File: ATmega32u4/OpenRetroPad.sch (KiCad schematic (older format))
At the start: 48 parts, among them J1 USB_B_Micro, J2 NRF24, J3 DB25_Female_MountingHoles, SW1 SW_Push, SW2 SW_Push, U1 AMS1117-3.3, U2 ATmega32U4, Y1 16MHz

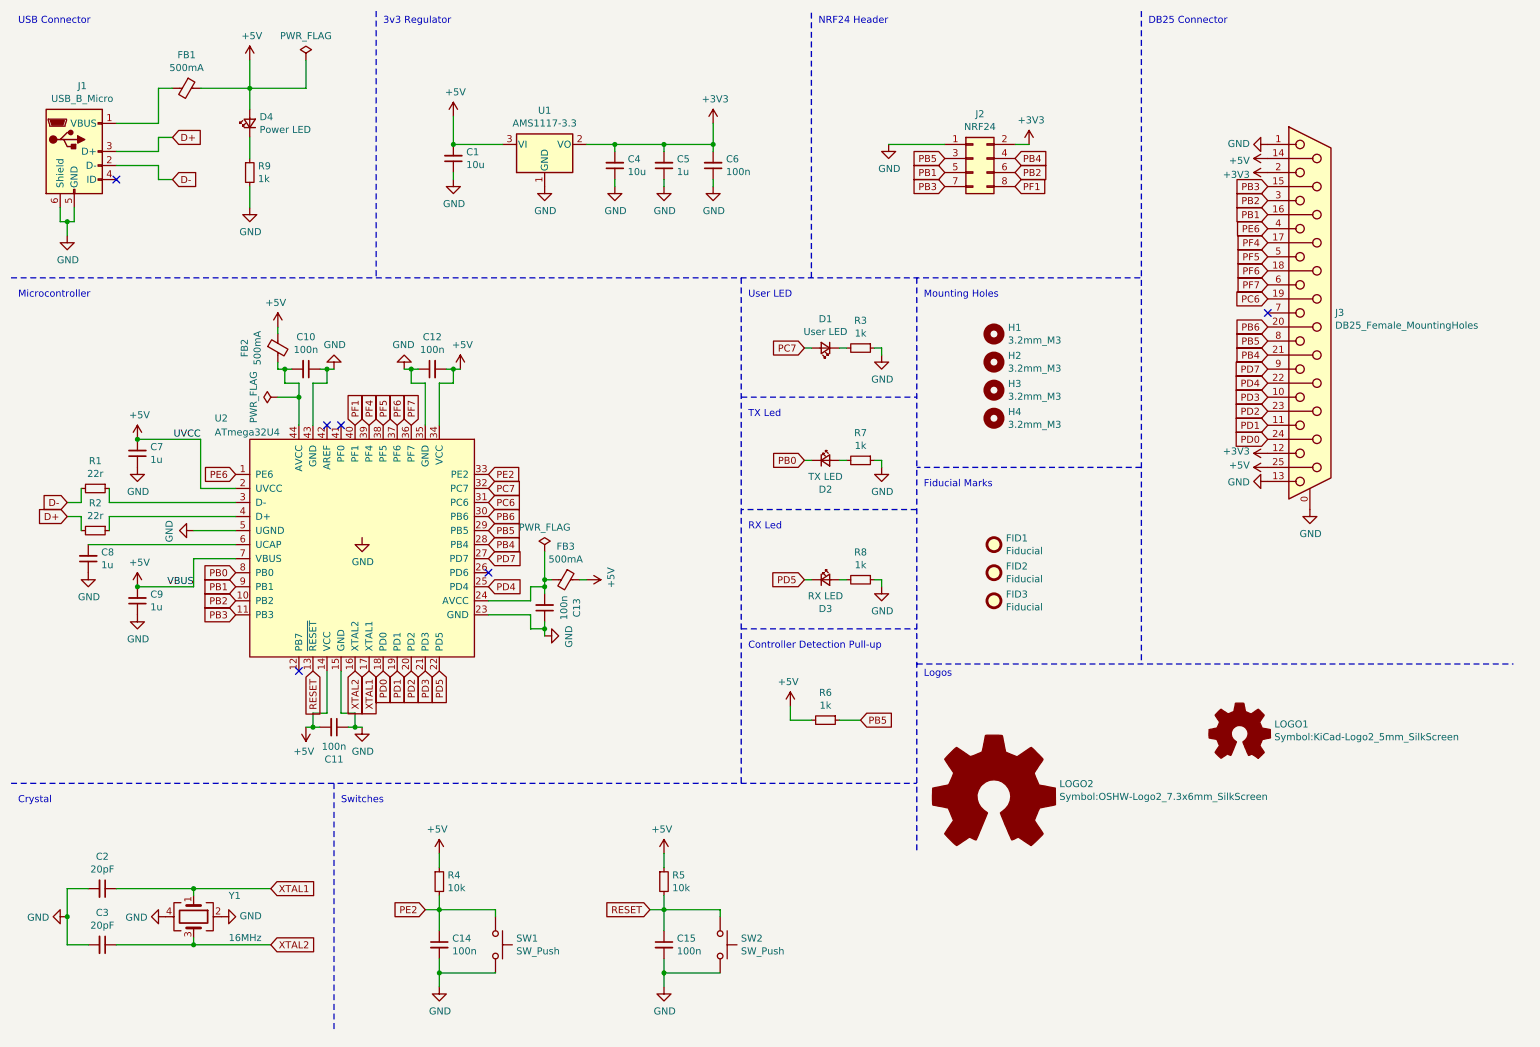
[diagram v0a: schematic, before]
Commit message: Update 2 layer board and use 0805 components, include outputs
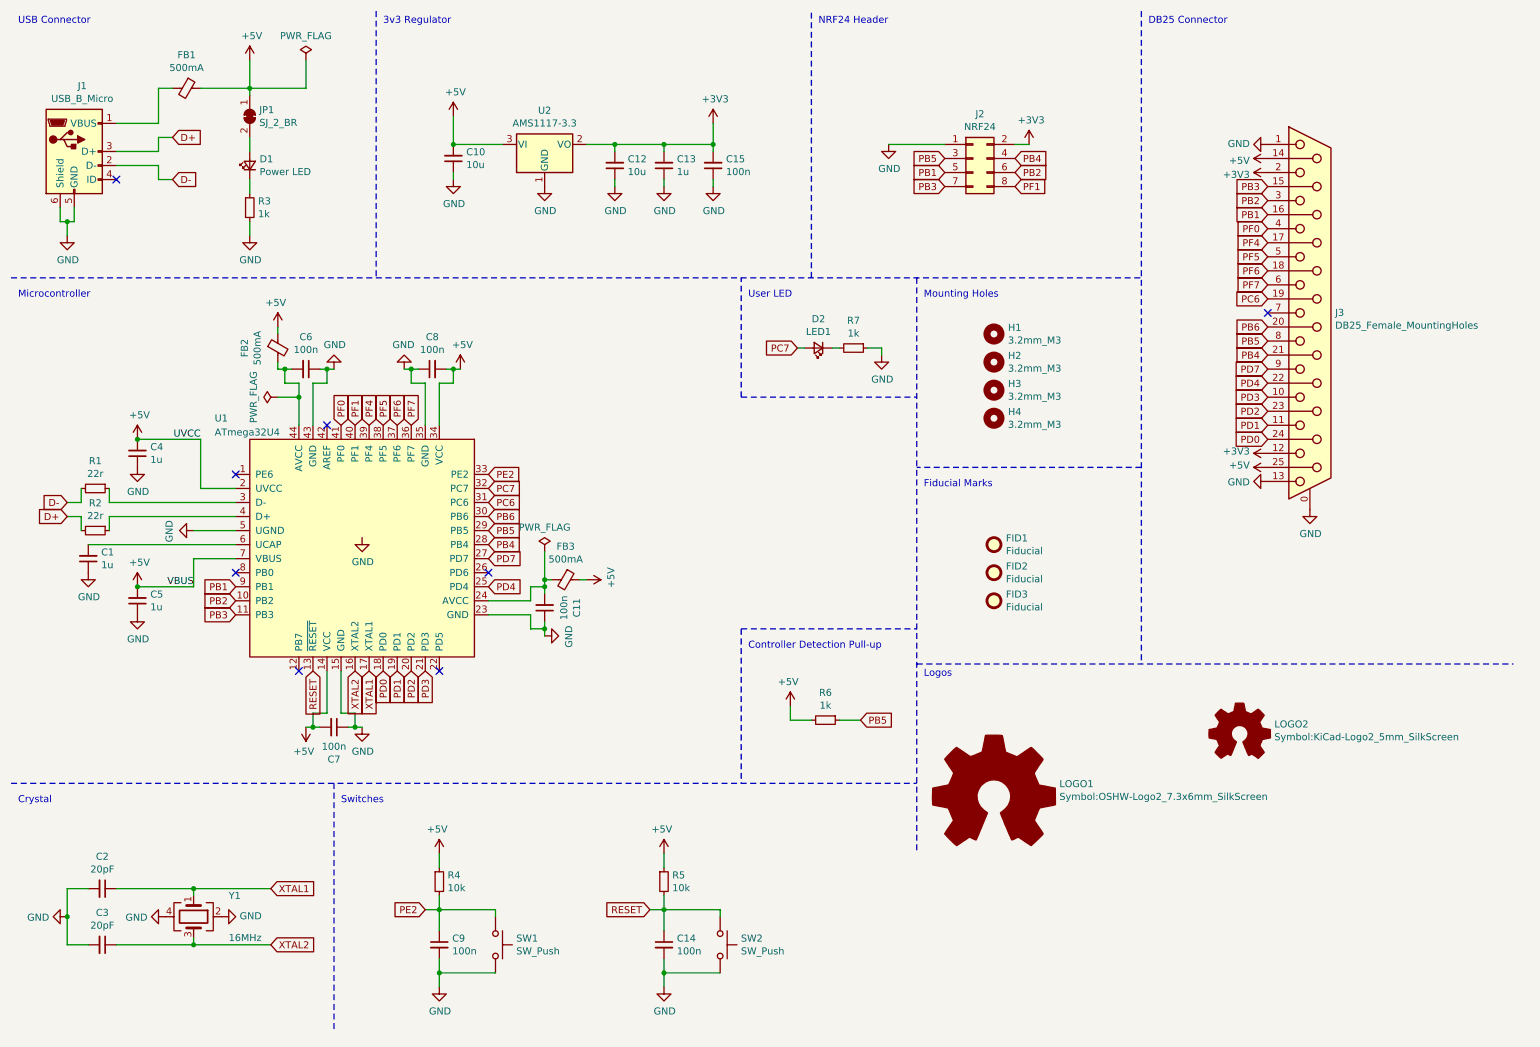
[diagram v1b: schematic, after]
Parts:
- removed D1: User LED, LED_SMD:LED_0603_1608Metric, symbol Device:LED_Small
- removed D3: RX LED, LED_SMD:LED_0603_1608Metric, symbol Device:LED_Small
- removed R7, R8: 1k, Resistor_SMD:R_0603_1608Metric, symbol Device:R_Small
- added JP1: SJ_2_BR, Jumper:SolderJumper-2_P1.3mm_Bridged_RoundedPad1.0x1.5mm, symbol Jumper:SolderJumper_2_Bridged
- C1: renamed from C8; footprint Capacitor_SMD:C_0603_1608Metric -> Capacitor_SMD:C_0805_2012Metric
- C11: renamed from C13; footprint Capacitor_SMD:C_0603_1608Metric -> Capacitor_SMD:C_0805_2012Metric
- C13: renamed from C5; footprint Capacitor_SMD:C_0603_1608Metric -> Capacitor_SMD:C_0805_2012Metric
- C14: renamed from C15; footprint Capacitor_SMD:C_0603_1608Metric -> Capacitor_SMD:C_0805_2012Metric
- C15: renamed from C6; footprint Capacitor_SMD:C_0603_1608Metric -> Capacitor_SMD:C_0805_2012Metric
- C2, C3: footprint Capacitor_SMD:C_0603_1608Metric -> Capacitor_SMD:C_0805_2012Metric
- C4: renamed from C7; footprint Capacitor_SMD:C_0603_1608Metric -> Capacitor_SMD:C_0805_2012Metric
- C5: renamed from C9; footprint Capacitor_SMD:C_0603_1608Metric -> Capacitor_SMD:C_0805_2012Metric
- C6: renamed from C10; footprint Capacitor_SMD:C_0603_1608Metric -> Capacitor_SMD:C_0805_2012Metric
- C7: renamed from C11; footprint Capacitor_SMD:C_0603_1608Metric -> Capacitor_SMD:C_0805_2012Metric
- C8: renamed from C12; footprint Capacitor_SMD:C_0603_1608Metric -> Capacitor_SMD:C_0805_2012Metric
- C9: renamed from C14; footprint Capacitor_SMD:C_0603_1608Metric -> Capacitor_SMD:C_0805_2012Metric
- D1: renamed from D4; footprint LED_SMD:LED_0603_1608Metric -> LED_SMD:LED_0805_2012Metric
- D2: value TX LED -> LED1; footprint LED_SMD:LED_0603_1608Metric -> LED_SMD:LED_0805_2012Metric
- FB2, FB3: footprint Inductor_SMD:L_0603_1608Metric -> Inductor_SMD:L_0805_2012Metric
- R1, R2, R4, R5, R6: footprint Resistor_SMD:R_0603_1608Metric -> Resistor_SMD:R_0805_2012Metric
- R3: renamed from R9; footprint Resistor_SMD:R_0603_1608Metric -> Resistor_SMD:R_0805_2012Metric
- R7: renamed from R3; footprint Resistor_SMD:R_0603_1608Metric -> Resistor_SMD:R_0805_2012Metric
- renumbered C1 to C10, C4 to C12, LOGO2 to LOGO1, LOGO1 to LOGO2, U2 to U1, U1 to U2
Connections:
- net +5V: now also JP1.1 (A); no longer D1.2 (A)
- net PC7: now also D2.2 (A)
- net PF0: now reaches U1.41 (PF0)
- net PF0: now also J3.4
- net at R7.2: now also D2.1 (K)
- net PB0: no longer names the net of U1.8 (PB0)
- net PB0: no longer D2.1 (K)
- net PD5: no longer names the net of U1.22 (PD5)
- net PE6: no longer names the net of U1.1 (PE6)
- net PE6: no longer J3.4
- new net: D1.2 (A), JP1.2 (B)
- no-connect marks 6 -> 8
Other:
- note removed: "RX Led"
- note removed: "TX Led"
- moved on the sheet: D1, R3, R7

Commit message: - Add on-board programmer - Micro USB -> USB-C
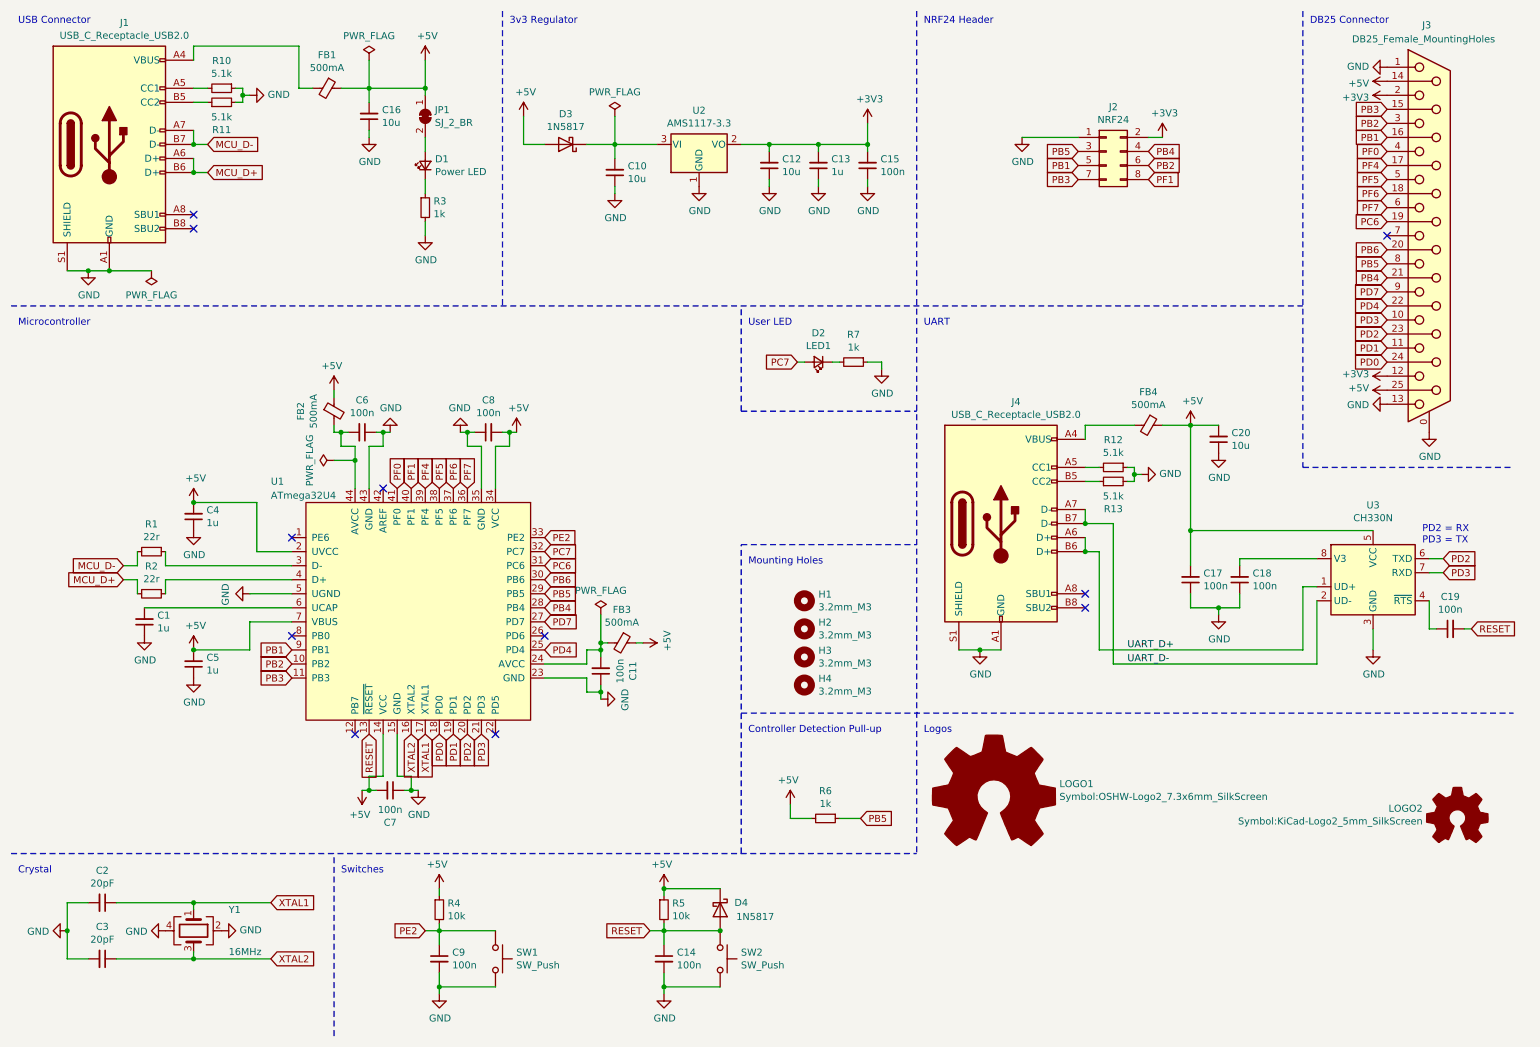
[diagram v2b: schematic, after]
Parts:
- removed FID1, FID2, FID3: Fiducial, OpenRetroPad:Fiducial_JLCPCB, symbol Mechanical:Fiducial
- removed J1: USB_B_Micro, OpenRetroPad:105017-0001, symbol Connector:USB_B_Micro
- added C16, C20: 10u, Capacitor_SMD:C_0805_2012Metric, symbol Device:C_Small
- added C17, C18, C19: 100n, Capacitor_SMD:C_0805_2012Metric, symbol Device:C_Small
- added D3, D4: 1N5817, Diode_SMD:D_SOD-323, symbol Diode:1N5817
- added FB4: 500mA, Inductor_SMD:L_0805_2012Metric, symbol Device:Ferrite_Bead_Small
- added J1, J4: USB_C_Receptacle_USB2.0, Connector_USB:USB_C_Receptacle_HRO_TYPE-C-31-M-12, symbol Connector:USB_C_Receptacle_USB2.0
- added R10, R11, R12, R13: 5.1k, Resistor_SMD:R_0805_2012Metric, symbol Device:R_Small
- added U3: CH330N, Package_SO:SOIC-8_3.9x4.9mm_P1.27mm, symbol Interface_USB:CH330N
- U1: footprint Package_DFN_QFN:QFN-44-1EP_7x7mm_P0.5mm_EP5.15x5.15mm_ThermalVias -> Package_QFP:TQFP-44_10x10mm_P0.8mm
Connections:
- net +5V: now also C16.2, C17.2, C20.2, D3.2 (A), D4.1 (K), FB4.1, U3.5 (VCC); no longer C10.2, U2.3 (VI)
- net GND: now also C16.1, C17.1, C18.1, C20.1, J1.A1 (GND), J1.A12 (GND), J1.B1 (GND), J1.B12 (GND), J1.S1 (SHIELD), J4.A1 (GND), J4.A12 (GND), J4.B1 (GND), J4.B12 (GND), J4.S1 (SHIELD), R10.1, R11.2, R12.1, R13.2, U3.3 (GND)
- net PD2: now also U3.6 (TXD)
- net PD3: now also U3.7 (RXD)
- net RESET: now also C19.2, D4.2 (A)
- net at FB1.2: now also J1.A4 (VBUS), J1.A9 (VBUS), J1.B4 (VBUS), J1.B9 (VBUS)
- net D+ renamed MCU_D+
- net MCU_D+: now also J1.A6 (D+), J1.B6 (D+)
- net D- renamed MCU_D-
- net MCU_D-: now also J1.A7 (D-), J1.B7 (D-)
- new net: C10.2, D3.1 (K), U2.3 (VI)
- new net: J1.A5 (CC1), R10.2
- new net: J1.B5 (CC2), R11.1
- new net: C19.1, U3.4 (~RTS)
- new net: C18.2, U3.8 (V3)
- new net: FB4.2, J4.A4 (VBUS), J4.A9 (VBUS), J4.B4 (VBUS), J4.B9 (VBUS)
- new net: J4.A5 (CC1), R12.2
- new net: J4.B5 (CC2), R13.1
- new net UART_D+: J4.A6 (D+), J4.B6 (D+), U3.1 (UD+)
- new net UART_D-: J4.A7 (D-), J4.B7 (D-), U3.2 (UD-)
- no-connect marks 8 -> 11
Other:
- note added: "PD2 = RX\nPD3 = TX"
- note added: "UART"
- note removed: "Fiducial Marks"
- moved on the sheet: C1, C10, C11, C12, C13, C14, C15, C2, C3, C4, C5, C6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
